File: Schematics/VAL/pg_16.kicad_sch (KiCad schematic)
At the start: 8 parts, among them U1801 XFBUF32, U1802 XFBUF32, U1803 XFBUF32, U1804 XFBUF32, U1805 XFBUF32, U1806 XFBUF32, U1807 XFBUF32, U1808 XFBUF32

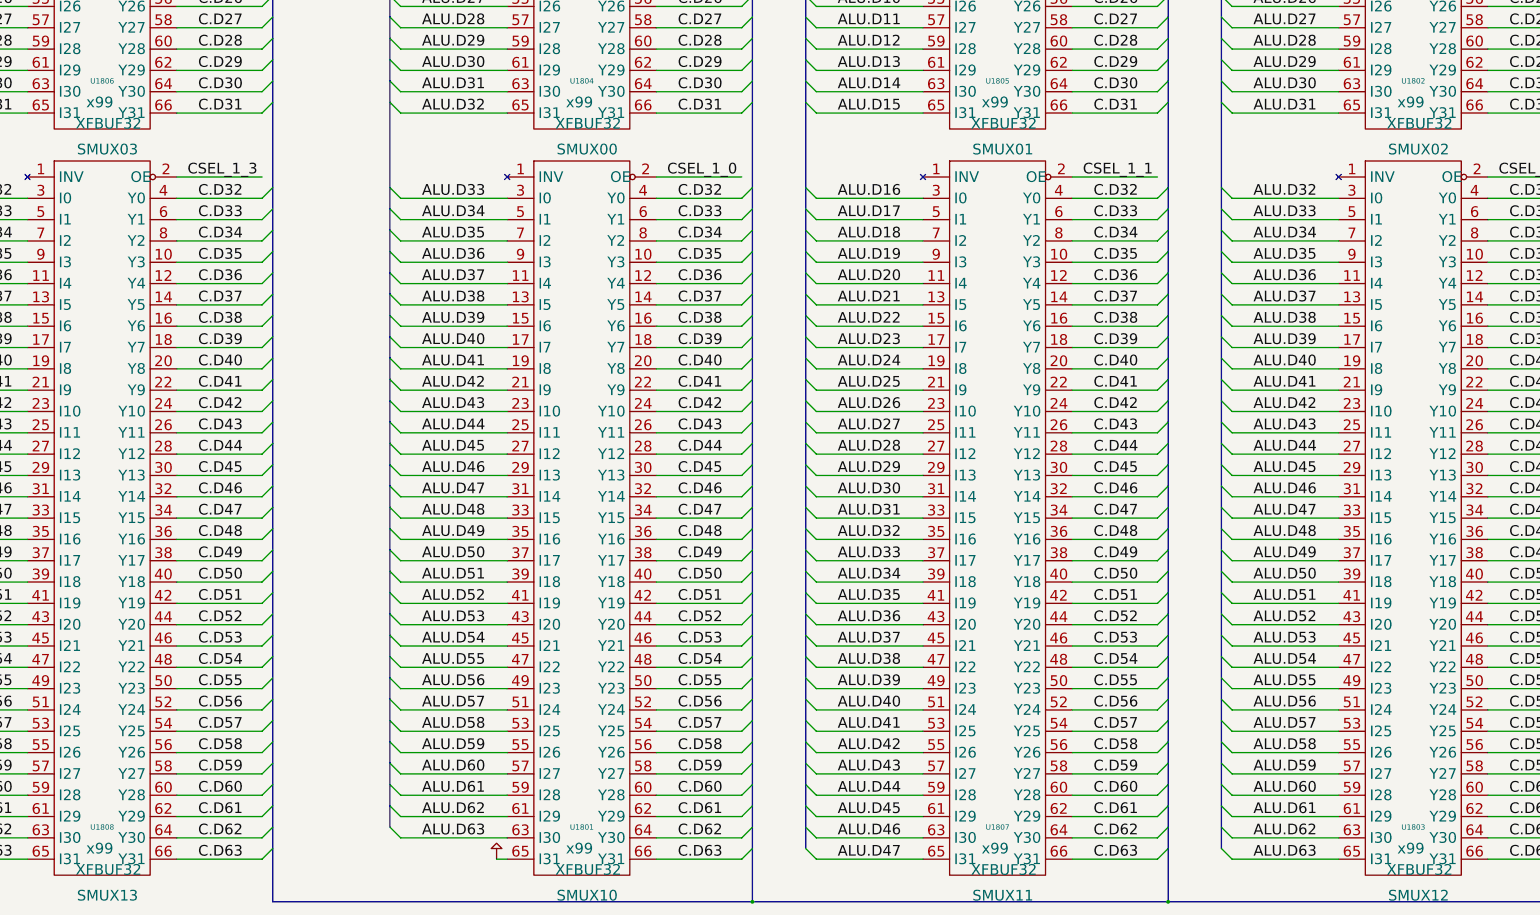
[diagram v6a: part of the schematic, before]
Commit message: Revert page 44 to older working (P2FP) version
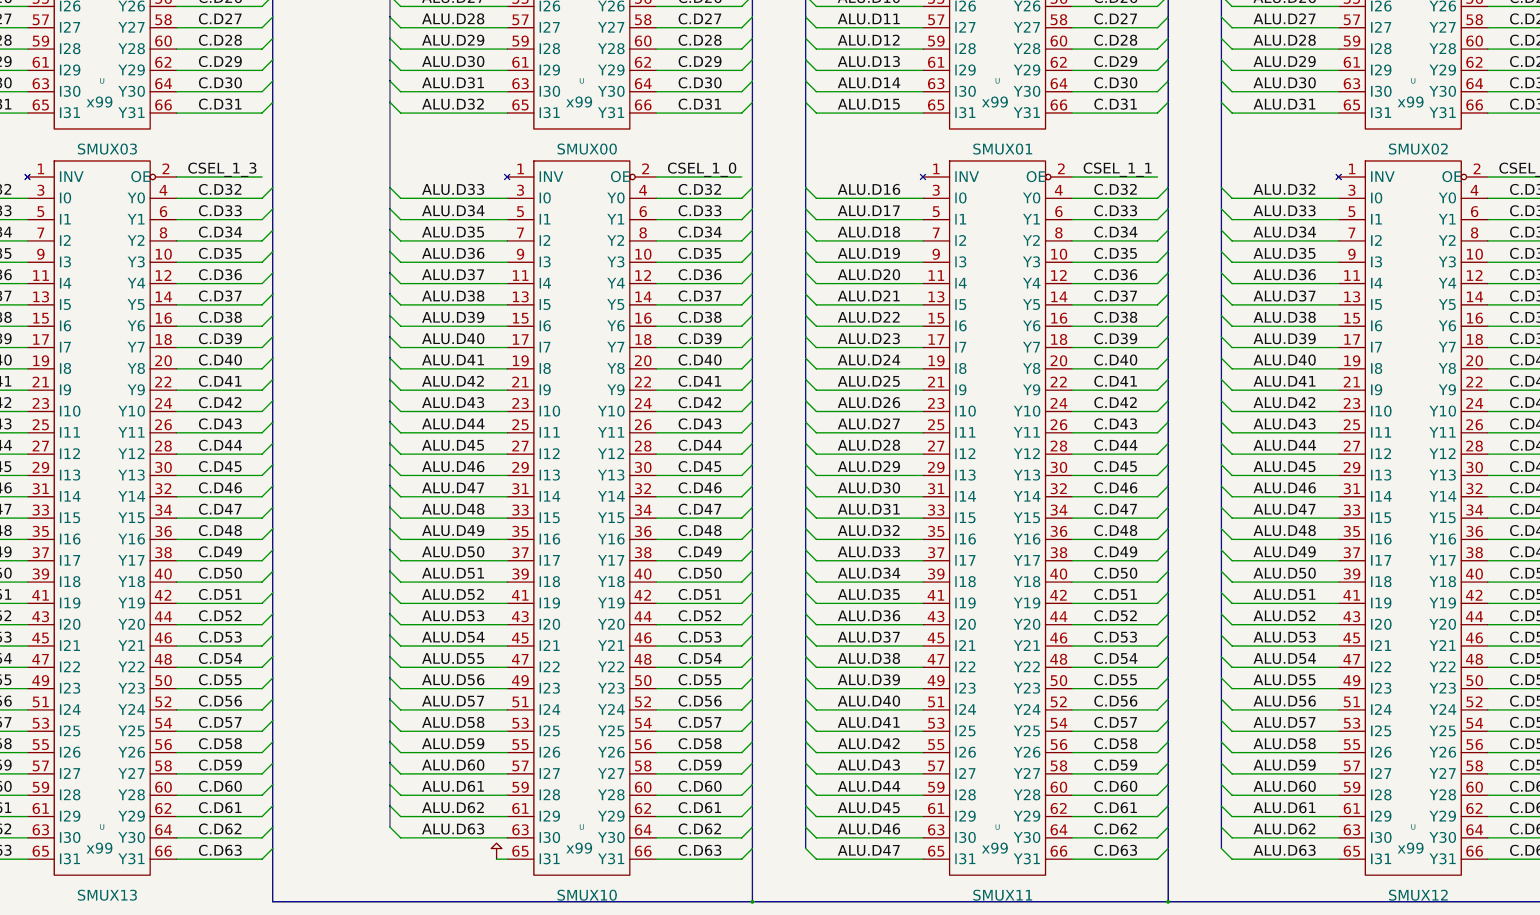
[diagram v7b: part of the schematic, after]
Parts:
- removed U1801, U1802, U1803, U1804, U1805, U1806, U1807, U1808: XFBUF32, symbol r1000:XFBUF32
- added U (x8): (no value), symbol r1000:XFBUF32
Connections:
- net ALU.D0: now also U.3 (I0), U.35 (I16)
- net ALU.D1: now also U.3 (I0), U.37 (I17), U.5 (I1)
- net ALU.D10: now also U.21 (I9), U.23 (I10), U.55 (I26)
- net ALU.D11: now also U.23 (I10), U.25 (I11), U.57 (I27)
- net ALU.D12: now also U.25 (I11), U.27 (I12), U.59 (I28)
- net ALU.D13: now also U.27 (I12), U.29 (I13), U.61 (I29)
- net ALU.D14: now also U.29 (I13), U.31 (I14), U.63 (I30)
- net ALU.D15: now also U.31 (I14), U.33 (I15), U.65 (I31)
- net ALU.D16: now also U.3 (I0), U.33 (I15), U.35 (I16)
- net ALU.D17: now also U.35 (I16), U.37 (I17), U.5 (I1)
- net ALU.D18: now also U.37 (I17), U.39 (I18), U.7 (I2)
- net ALU.D19: now also U.39 (I18), U.41 (I19), U.9 (I3)
- net ALU.D2: now also U.39 (I18), U.5 (I1), U.7 (I2)
- net ALU.D20: now also U.11 (I4), U.41 (I19), U.43 (I20)
- net ALU.D21: now also U.13 (I5), U.43 (I20), U.45 (I21)
- net ALU.D22: now also U.15 (I6), U.45 (I21), U.47 (I22)
- net ALU.D23: now also U.17 (I7), U.47 (I22), U.49 (I23)
- net ALU.D24: now also U.19 (I8), U.49 (I23), U.51 (I24)
- net ALU.D25: now also U.21 (I9), U.51 (I24), U.53 (I25)
- net ALU.D26: now also U.23 (I10), U.53 (I25), U.55 (I26)
- net ALU.D27: now also U.25 (I11), U.55 (I26), U.57 (I27)
- net ALU.D28: now also U.27 (I12), U.57 (I27), U.59 (I28)
- net ALU.D29: now also U.29 (I13), U.59 (I28), U.61 (I29)
- net ALU.D3: now also U.41 (I19), U.7 (I2), U.9 (I3)
- net ALU.D30: now also U.31 (I14), U.61 (I29), U.63 (I30)
- net ALU.D31: now also U.33 (I15), U.63 (I30), U.65 (I31)
- net ALU.D32: now also U.3 (I0), U.35 (I16), U.65 (I31)
- net ALU.D33: now also U.3 (I0), U.37 (I17), U.5 (I1)
- net ALU.D34: now also U.39 (I18), U.5 (I1), U.7 (I2)
- net ALU.D35: now also U.41 (I19), U.7 (I2), U.9 (I3)
- net ALU.D36: now also U.11 (I4), U.43 (I20), U.9 (I3)
- net ALU.D37: now also U.11 (I4), U.13 (I5), U.45 (I21)
- net ALU.D38: now also U.13 (I5), U.15 (I6), U.47 (I22)
- net ALU.D39: now also U.15 (I6), U.17 (I7), U.49 (I23)
- net ALU.D4: now also U.11 (I4), U.43 (I20), U.9 (I3)
- net ALU.D40: now also U.17 (I7), U.19 (I8), U.51 (I24)
- net ALU.D41: now also U.19 (I8), U.21 (I9), U.53 (I25)
- net ALU.D42: now also U.21 (I9), U.23 (I10), U.55 (I26)
- net ALU.D43: now also U.23 (I10), U.25 (I11), U.57 (I27)
- net ALU.D44: now also U.25 (I11), U.27 (I12), U.59 (I28)
- net ALU.D45: now also U.27 (I12), U.29 (I13), U.61 (I29)
- net ALU.D46: now also U.29 (I13), U.31 (I14), U.63 (I30)
- net ALU.D47: now also U.31 (I14), U.33 (I15), U.65 (I31)
- net ALU.D48: now also U.33 (I15), U.35 (I16)
- net ALU.D49: now also U.35 (I16), U.37 (I17)
- net ALU.D5: now also U.11 (I4), U.13 (I5), U.45 (I21)
- net ALU.D50: now also U.37 (I17), U.39 (I18)
- net ALU.D51: now also U.39 (I18), U.41 (I19)
- net ALU.D52: now also U.41 (I19), U.43 (I20)
- net ALU.D53: now also U.43 (I20), U.45 (I21)
- net ALU.D54: now also U.45 (I21), U.47 (I22)
- net ALU.D55: now also U.47 (I22), U.49 (I23)
- net ALU.D56: now also U.49 (I23), U.51 (I24)
- net ALU.D57: now also U.51 (I24), U.53 (I25)
- net ALU.D58: now also U.53 (I25), U.55 (I26)
- net ALU.D59: now also U.55 (I26), U.57 (I27)
- net ALU.D6: now also U.13 (I5), U.15 (I6), U.47 (I22)
- net ALU.D60: now also U.57 (I27), U.59 (I28)
- net ALU.D61: now also U.59 (I28), U.61 (I29)
- net ALU.D62: now also U.61 (I29), U.63 (I30)
- net ALU.D63: now also U.63 (I30), U.65 (I31)
- net ALU.D7: now also U.15 (I6), U.17 (I7), U.49 (I23)
- net ALU.D8: now also U.17 (I7), U.19 (I8), U.51 (I24)
- net ALU.D9: now also U.19 (I8), U.21 (I9), U.53 (I25)
- net C.D0: now also U.4 (Y0), U.4 (Y0), U.4 (Y0), U.4 (Y0)
- net C.D1: now also U.6 (Y1), U.6 (Y1), U.6 (Y1), U.6 (Y1)
- net C.D10: now also U.24 (Y10), U.24 (Y10), U.24 (Y10), U.24 (Y10)
- net C.D11: now also U.26 (Y11), U.26 (Y11), U.26 (Y11), U.26 (Y11)
- net C.D12: now also U.28 (Y12), U.28 (Y12), U.28 (Y12), U.28 (Y12)
- net C.D13: now also U.30 (Y13), U.30 (Y13), U.30 (Y13), U.30 (Y13)
- net C.D14: now also U.32 (Y14), U.32 (Y14), U.32 (Y14), U.32 (Y14)
- net C.D15: now also U.34 (Y15), U.34 (Y15), U.34 (Y15), U.34 (Y15)
- net C.D16: now also U.36 (Y16), U.36 (Y16), U.36 (Y16), U.36 (Y16)
- net C.D17: now also U.38 (Y17), U.38 (Y17), U.38 (Y17), U.38 (Y17)
- net C.D18: now also U.40 (Y18), U.40 (Y18), U.40 (Y18), U.40 (Y18)
- net C.D19: now also U.42 (Y19), U.42 (Y19), U.42 (Y19), U.42 (Y19)
- net C.D2: now also U.8 (Y2), U.8 (Y2), U.8 (Y2), U.8 (Y2)
- net C.D20: now also U.44 (Y20), U.44 (Y20), U.44 (Y20), U.44 (Y20)
- net C.D21: now also U.46 (Y21), U.46 (Y21), U.46 (Y21), U.46 (Y21)
- net C.D22: now also U.48 (Y22), U.48 (Y22), U.48 (Y22), U.48 (Y22)
- net C.D23: now also U.50 (Y23), U.50 (Y23), U.50 (Y23), U.50 (Y23)
- net C.D24: now also U.52 (Y24), U.52 (Y24), U.52 (Y24), U.52 (Y24)
- net C.D25: now also U.54 (Y25), U.54 (Y25), U.54 (Y25), U.54 (Y25)
- net C.D26: now also U.56 (Y26), U.56 (Y26), U.56 (Y26), U.56 (Y26)
- net C.D27: now also U.58 (Y27), U.58 (Y27), U.58 (Y27), U.58 (Y27)
- net C.D28: now also U.60 (Y28), U.60 (Y28), U.60 (Y28), U.60 (Y28)
- net C.D29: now also U.62 (Y29), U.62 (Y29), U.62 (Y29), U.62 (Y29)
- net C.D3: now also U.10 (Y3), U.10 (Y3), U.10 (Y3), U.10 (Y3)
- net C.D30: now also U.64 (Y30), U.64 (Y30), U.64 (Y30), U.64 (Y30)
- net C.D31: now also U.66 (Y31), U.66 (Y31), U.66 (Y31), U.66 (Y31)
- net C.D32: now also U.4 (Y0), U.4 (Y0), U.4 (Y0), U.4 (Y0)
- net C.D33: now also U.6 (Y1), U.6 (Y1), U.6 (Y1), U.6 (Y1)
- net C.D34: now also U.8 (Y2), U.8 (Y2), U.8 (Y2), U.8 (Y2)
- net C.D35: now also U.10 (Y3), U.10 (Y3), U.10 (Y3), U.10 (Y3)
- net C.D36: now also U.12 (Y4), U.12 (Y4), U.12 (Y4), U.12 (Y4)
- net C.D37: now also U.14 (Y5), U.14 (Y5), U.14 (Y5), U.14 (Y5)
- net C.D38: now also U.16 (Y6), U.16 (Y6), U.16 (Y6), U.16 (Y6)
- net C.D39: now also U.18 (Y7), U.18 (Y7), U.18 (Y7), U.18 (Y7)
- net C.D4: now also U.12 (Y4), U.12 (Y4), U.12 (Y4), U.12 (Y4)
- net C.D40: now also U.20 (Y8), U.20 (Y8), U.20 (Y8), U.20 (Y8)
- net C.D41: now also U.22 (Y9), U.22 (Y9), U.22 (Y9), U.22 (Y9)
- net C.D42: now also U.24 (Y10), U.24 (Y10), U.24 (Y10), U.24 (Y10)
- net C.D43: now also U.26 (Y11), U.26 (Y11), U.26 (Y11), U.26 (Y11)
- net C.D44: now also U.28 (Y12), U.28 (Y12), U.28 (Y12), U.28 (Y12)
- net C.D45: now also U.30 (Y13), U.30 (Y13), U.30 (Y13), U.30 (Y13)
- net C.D46: now also U.32 (Y14), U.32 (Y14), U.32 (Y14), U.32 (Y14)
- net C.D47: now also U.34 (Y15), U.34 (Y15), U.34 (Y15), U.34 (Y15)
- net C.D48: now also U.36 (Y16), U.36 (Y16), U.36 (Y16), U.36 (Y16)
- net C.D49: now also U.38 (Y17), U.38 (Y17), U.38 (Y17), U.38 (Y17)
- net C.D5: now also U.14 (Y5), U.14 (Y5), U.14 (Y5), U.14 (Y5)
- net C.D50: now also U.40 (Y18), U.40 (Y18), U.40 (Y18), U.40 (Y18)
- net C.D51: now also U.42 (Y19), U.42 (Y19), U.42 (Y19), U.42 (Y19)
- net C.D52: now also U.44 (Y20), U.44 (Y20), U.44 (Y20), U.44 (Y20)
- net C.D53: now also U.46 (Y21), U.46 (Y21), U.46 (Y21), U.46 (Y21)
- net C.D54: now also U.48 (Y22), U.48 (Y22), U.48 (Y22), U.48 (Y22)
- net C.D55: now also U.50 (Y23), U.50 (Y23), U.50 (Y23), U.50 (Y23)
- net C.D56: now also U.52 (Y24), U.52 (Y24), U.52 (Y24), U.52 (Y24)
- net C.D57: now also U.54 (Y25), U.54 (Y25), U.54 (Y25), U.54 (Y25)
- net C.D58: now also U.56 (Y26), U.56 (Y26), U.56 (Y26), U.56 (Y26)
- net C.D59: now also U.58 (Y27), U.58 (Y27), U.58 (Y27), U.58 (Y27)
- net C.D6: now also U.16 (Y6), U.16 (Y6), U.16 (Y6), U.16 (Y6)
- net C.D60: now also U.60 (Y28), U.60 (Y28), U.60 (Y28), U.60 (Y28)
- net C.D61: now also U.62 (Y29), U.62 (Y29), U.62 (Y29), U.62 (Y29)
- net C.D62: now also U.64 (Y30), U.64 (Y30), U.64 (Y30), U.64 (Y30)
- net C.D63: now also U.66 (Y31), U.66 (Y31), U.66 (Y31), U.66 (Y31)
- net C.D7: now also U.18 (Y7), U.18 (Y7), U.18 (Y7), U.18 (Y7)
- net C.D8: now also U.20 (Y8), U.20 (Y8), U.20 (Y8), U.20 (Y8)
- net C.D9: now also U.22 (Y9), U.22 (Y9), U.22 (Y9), U.22 (Y9)
- net CSEL_0_0: now also U.2 (OE)
- net CSEL_0_1: now also U.2 (OE)
- net CSEL_0_2: now also U.2 (OE)
- net CSEL_0_3: now also U.2 (OE)
- net CSEL_1_0: now also U.2 (OE)
- net CSEL_1_1: now also U.2 (OE)
- net CSEL_1_2: now also U.2 (OE)
- net CSEL_1_3: now also U.2 (OE)
- net PU: now also U.11 (I4), U.13 (I5), U.15 (I6), U.17 (I7), U.19 (I8), U.21 (I9), U.23 (I10), U.25 (I11), U.27 (I12), U.29 (I13), U.3 (I0), U.31 (I14), U.33 (I15), U.5 (I1), U.65 (I31), U.7 (I2), U.9 (I3)
- net WDR.D0: now also U.3 (I0)
- net WDR.D1: now also U.5 (I1)
- net WDR.D10: now also U.23 (I10)
- net WDR.D11: now also U.25 (I11)
- net WDR.D12: now also U.27 (I12)
- net WDR.D13: now also U.29 (I13)
- net WDR.D14: now also U.31 (I14)
- net WDR.D15: now also U.33 (I15)
- net WDR.D16: now also U.35 (I16)
- net WDR.D17: now also U.37 (I17)
- net WDR.D18: now also U.39 (I18)
- net WDR.D19: now also U.41 (I19)
- net WDR.D2: now also U.7 (I2)
- net WDR.D20: now also U.43 (I20)
- net WDR.D21: now also U.45 (I21)
- net WDR.D22: now also U.47 (I22)
- net WDR.D23: now also U.49 (I23)
- net WDR.D24: now also U.51 (I24)
- net WDR.D25: now also U.53 (I25)
- net WDR.D26: now also U.55 (I26)
- net WDR.D27: now also U.57 (I27)
- net WDR.D28: now also U.59 (I28)
- net WDR.D29: now also U.61 (I29)
- net WDR.D3: now also U.9 (I3)
- net WDR.D30: now also U.63 (I30)
- net WDR.D31: now also U.65 (I31)
- net WDR.D32: now also U.3 (I0)
- net WDR.D33: now also U.5 (I1)
- net WDR.D34: now also U.7 (I2)
- net WDR.D35: now also U.9 (I3)
- net WDR.D36: now also U.11 (I4)
- net WDR.D37: now also U.13 (I5)
- net WDR.D38: now also U.15 (I6)
- net WDR.D39: now also U.17 (I7)
- net WDR.D4: now also U.11 (I4)
- net WDR.D40: now also U.19 (I8)
- net WDR.D41: now also U.21 (I9)
- net WDR.D42: now also U.23 (I10)
- net WDR.D43: now also U.25 (I11)
- net WDR.D44: now also U.27 (I12)
- net WDR.D45: now also U.29 (I13)
- net WDR.D46: now also U.31 (I14)
- net WDR.D47: now also U.33 (I15)
- net WDR.D48: now also U.35 (I16)
- net WDR.D49: now also U.37 (I17)
- net WDR.D5: now also U.13 (I5)
- net WDR.D50: now also U.39 (I18)
- net WDR.D51: now also U.41 (I19)
- net WDR.D52: now also U.43 (I20)
- net WDR.D53: now also U.45 (I21)
- net WDR.D54: now also U.47 (I22)
- net WDR.D55: now also U.49 (I23)
- net WDR.D56: now also U.51 (I24)
- net WDR.D57: now also U.53 (I25)
- net WDR.D58: now also U.55 (I26)
- net WDR.D59: now also U.57 (I27)
- net WDR.D6: now also U.15 (I6)
- net WDR.D60: now also U.59 (I28)
- net WDR.D61: now also U.61 (I29)
- net WDR.D62: now also U.63 (I30)
- net WDR.D63: now also U.65 (I31)
- net WDR.D7: now also U.17 (I7)
- net WDR.D8: now also U.19 (I8)
- net WDR.D9: now also U.21 (I9)
